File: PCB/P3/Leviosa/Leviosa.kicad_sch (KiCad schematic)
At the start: 56 parts, among them J1 Barrel_Jack, J2 2.54mm 1x03 Spare

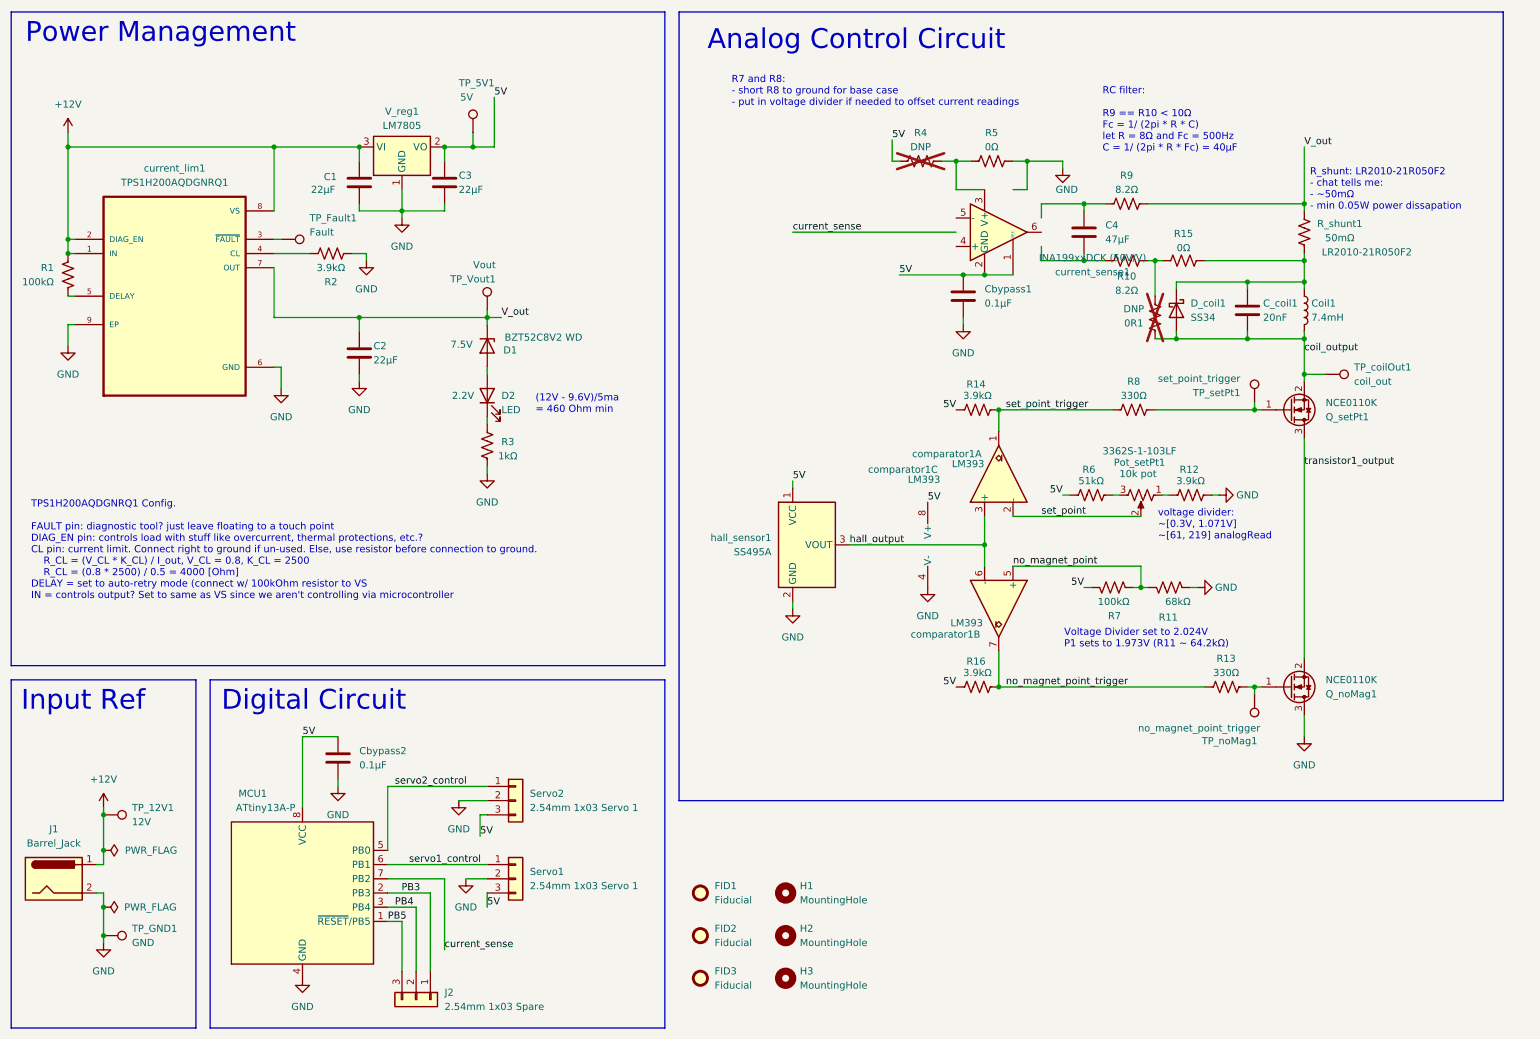
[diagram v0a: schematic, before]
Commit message: Pcb/p3 (#19)
* first pass on P3 of PCB

* shift parts in schematic

* update circuit with 0R on comparator output & servo pinout

* fix name

* add unity buffer op amp

* update schematic with single instrumental amplifier (instead of double)

* fix naming of folders

* update node names

* create PCB initial draft

* update PCB and schematic slightly

* Update - Dec 9th

- Updated labels for power, components and TPs
- Changed standard comp to 0603 knowing we have these
- Updated TPS symbol

* Board revised

- Big change from the last so have a look over

* added status led for coil and moved components groups closer together

* add 0.1uF cap to gate driver VCC

* update H1 pos

* add via

* gerbers created

* updated schematic for usb and i2s

* Update Leviosa.kicad_pro

---------

Co-authored-by: AirMatress <134566567+AirMatress@users.noreply.github.com>
Co-authored-by: Jack <134566567+Kay-Jack@users.noreply.github.com>
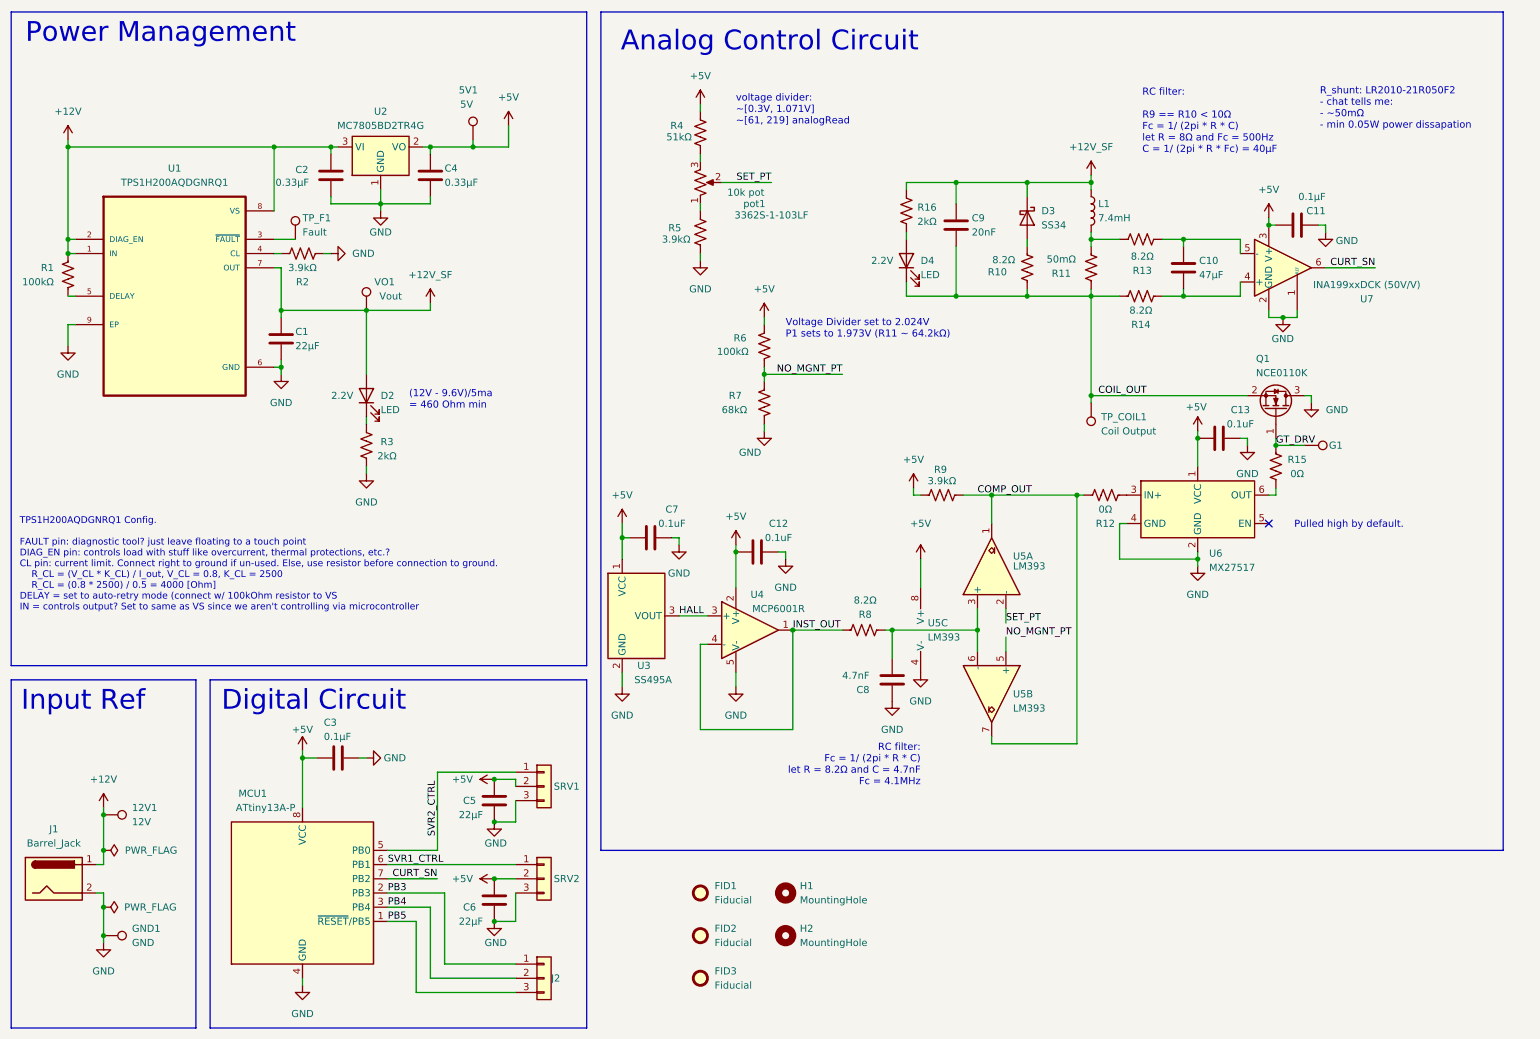
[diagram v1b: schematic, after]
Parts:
- removed 0R1, R4: DNP, Resistor_SMD:R_0603_1608Metric, symbol Device:R_US
- removed D1: BZT52C8V2 WD, Diode_SMD:D_SOD-123, symbol Device:D_Zener
- removed H3: MountingHole, MountingHole:MountingHole_3.2mm_M3_ISO7380, symbol Mechanical:MountingHole
- removed Q_noMag1: NCE0110K, Package_TO_SOT_SMD:TO-252-2, symbol Transistor_FET:DMN61D8LQ
- removed R13: 330Ω, Resistor_SMD:R_0805_2012Metric_Pad1.20x1.40mm_HandSolder, symbol Device:R_US
- removed R5: 0Ω, Resistor_SMD:R_0603_1608Metric, symbol Device:R_US
- removed TP_noMag1: no_magnet_point_trigger, TestPoint:TestPoint_Pad_D1.5mm, symbol Connector:TestPoint
- added C12, C13, C7: 0.1uF, Capacitor_SMD:C_0603_1608Metric, symbol Device:C
- added C5, C6: 22µF, Capacitor_SMD:C_0805_2012Metric, symbol Device:C
- added C8: 4.7nF, Capacitor_SMD:C_0805_2012Metric_Pad1.18x1.45mm_HandSolder, symbol Device:C
- added D4: LED, LED_SMD:LED_0805_2012Metric, symbol Device:LED
- added R10: 8.2Ω, Resistor_SMD:R_1206_3216Metric, symbol Device:R_US
- added R12: 0Ω, Resistor_SMD:R_0603_1608Metric, symbol Device:R_US
- added U4: MCP6001R, Package_TO_SOT_SMD:SOT-23-5, symbol Amplifier_Operational:MCP6001R
- added U6: MX27517, Package_TO_SOT_SMD:SOT-23-6, symbol Driver_FET:ZXGD3001E6
- 12V1: renamed from TP_12V1; footprint TestPoint:TestPoint_Pad_D1.5mm -> TestPoint:TestPoint_Pad_D1.0mm
- C11: renamed from Cbypass1; footprint Capacitor_SMD:C_0402_1005Metric -> Capacitor_SMD:C_0603_1608Metric
- C2: renamed from C1; value 22µF -> 0.33µF
- C3: renamed from Cbypass2; footprint Capacitor_SMD:C_0402_1005Metric -> Capacitor_SMD:C_0603_1608Metric
- C4: renamed from C3; value 22µF -> 0.33µF
- D3: renamed from D_coil1; footprint Diode_SMD:D_SMA -> Diode_SMD:D_SOD-323
- G1: renamed from TP_setPt1; footprint TestPoint:TestPoint_Pad_D1.5mm -> TestPoint:TestPoint_Pad_D1.0mm
- GND1: renamed from TP_GND1; footprint TestPoint:TestPoint_Pad_D1.5mm -> TestPoint:TestPoint_Pad_D1.0mm
- L1: renamed from Coil1; footprint Inductor_THT:L_Axial_L5.0mm_D3.6mm_P10.00mm_Horizontal_Murata_BL01RN1A2A2 -> Connector_PinHeader_2.54mm:PinHeader_2x01_P2.54mm_Vertical
- R1: footprint Resistor_SMD:R_0805_2012Metric_Pad1.20x1.40mm_HandSolder -> Resistor_SMD:R_0603_1608Metric
- R15: Link (none) -> https://jlcpcb.com/partdetail/18710-1206W4F820KT5E/C18022
- R16: value 3.9kΩ -> 2kΩ; Link https://jlcpcb.com/partdetail/23745-0603WAF3901T5E/C23018 -> (none)
- R3: value 1kΩ -> 2kΩ; footprint Resistor_SMD:R_0805_2012Metric_Pad1.20x1.40mm_HandSolder -> Resistor_SMD:R_0603_1608Metric
- R6: renamed from R7; footprint Resistor_SMD:R_0805_2012Metric_Pad1.20x1.40mm_HandSolder -> Resistor_SMD:R_0603_1608Metric
- R8: value 330Ω -> 8.2Ω; footprint Resistor_SMD:R_0805_2012Metric_Pad1.20x1.40mm_HandSolder -> Resistor_SMD:R_1206_3216Metric; Link (none) -> https://jlcpcb.com/partdetail/18710-1206W4F820KT5E/C18022
- TP_COIL1: renamed from TP_coilOut1; value coil_out -> Coil Output; footprint TestPoint:TestPoint_Pad_D1.5mm -> TestPoint:TestPoint_Pad_D1.0mm
- TP_F1: renamed from TP_Fault1; footprint TestPoint:TestPoint_Pad_D1.5mm -> TestPoint:TestPoint_Pad_D1.0mm
- U1: renamed from current_lim1; footprint TPS1H200AQDGNRQ1:SOP65P490X110-9N -> Package_SO:HVSSOP-8-1EP_3x3mm_P0.65mm_EP1.57x1.89mm; MF Texas Instruments -> (none); MP TPS1H200AQDGNRQ1 -> (none); PACKAGE HVSSOP-8 Texas Instruments -> (none); PRICE None -> (none); PURCHASE-URL https://www.snapeda.com/api/url_track_click_mouser/?unipart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 -> (none); SNAPEDA_LINK https://www.snapeda.com/parts/TPS1H200AQDGNRQ1/Texas+Instru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 -> (none)
- U2: renamed from V_reg1; value LM7805 -> MC7805BD2TR4G; footprint Package_TO_SOT_SMD:SOT-223-3_TabPin2 -> Package_TO_SOT_SMD:TO-263-2; Link (none) -> https://jlcpcb.com/partdetail/onsemi-MC7805BD2TR4G/C15833
- U5: renamed from comparator1; footprint Package_SO:SOIC-8_5.3x5.3mm_P1.27mm -> Package_SO:SOIC-8_3.9x4.9mm_P1.27mm; Link (none) -> https://jlcpcb.com/partdetail/onsemi-LM393DR2G/C7955
- VO1: renamed from TP_Vout1; footprint TestPoint:TestPoint_Pad_D1.5mm -> TestPoint:TestPoint_Pad_D1.0mm
- renumbered TP_5V1 to 5V1, C2 to C1, C4 to C10, C_coil1 to C9, Q_setPt1 to Q1, R_shunt1 to R11, R10 to R13, R9 to R14, R6 to R4, R12 to R5, R11 to R7, R14 to R9, Servo2 to SRV1, Servo1 to SRV2, hall_sensor1 to U3, current_sense1 to U7, Pot_setPt1 to pot1
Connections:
- net current_sense is gone; now on net CURT_SN: MCU1.7 (PB2)
- net transistor1_output is gone; now on net GND: Q1.3 (D)
- net GND: now also SRV1.3 (Pin_3), SRV2.3 (Pin_3), U7.1 (REF), U7.2 (GND), C12.2, C13.2, C5.2, C6.2, C7.2, C8.1, U4.5 (V-), U6.2 (GND), U6.4 (GND); no longer SRV1.2 (Pin_2), SRV2.2 (Pin_2)
- net at R13.1: now also L1.2, R11.1; no longer R15.2
- net at C10.2, R13.2: now also U7.5 (-)
- net +12V_SF: now reaches C9.1, D3.1 (K), L1.1
- net +12V_SF: now also C1.1, D2.2 (A), R16.1, U1.7 (OUT), VO1.1; no longer R11.1, R15.1
- net +5V: now reaches U7.3 (V+)
- net +5V: now also 5V1.1, C11.1, C3.1, C4.1, MCU1.8 (VCC), R4.2, R6.2, R9.2, SRV1.2 (Pin_2), SRV2.2 (Pin_2), U2.2 (VO), U3.1 (VCC), U5.8 (V+), C12.1, C13.1, C5.1, C6.1, C7.1, U4.2 (V+), U6.1 (VCC)
- net at U7.4 (+): now also C10.1, R14.2
- net CURT_SN: now reaches U7.6
- net GT_DRV: now reaches G1.1, Q1.1 (G)
- net GT_DRV: now also R15.2; no longer R8.1
- removed net 5V: 5V1.1, C11.1, C3.1, C4.1, MCU1.8 (VCC), R16.2, R4.2, R6.2, R9.2, SRV1.3 (Pin_3), SRV2.3 (Pin_3), U2.2 (VO), U3.1 (VCC), U5.8 (V+), U7.1 (REF), U7.2 (GND)
- removed net V_out: C1.1, R11.2, R14.1, U1.7 (OUT), VO1.1
- net coil_output renamed COIL_OUT
- net COIL_OUT: now also R11.2, R14.1, D4.1 (K), R10.2; no longer D3.2 (A), L1.2
- net hall_output: no longer names the net of U5.3 (+), U5.6 (-)
- net hall_output: now also R8.2, C8.2; no longer U3.3 (VOUT)
- net no_magnet_point renamed NO_MGNT_PT
- net no_magnet_point_trigger renamed COMP_OUT
- net COMP_OUT: now also R9.1, U5.1, R12.1; no longer R16.1
- net servo1_control renamed SVR1_CTRL
- net servo2_control renamed SVR2_CTRL
- net set_point renamed SET_PT
- removed net set_point_trigger: R8.2, R9.1, U5.1
- new net: D4.2 (A), R16.2
- new net: R12.2, U6.3 (IN+)
- new net: R15.1, U6.6 (OUT)
- new net: D3.2 (A), R10.1
- new net HALL: U3.3 (VOUT), U4.3 (+)
- new net INST_OUT: R8.1, U4.1, U4.4 (-)
- no-connect marks 0 -> 1
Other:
- note added: "Pulled high by default."
- note added: "RC filter: Fc = 1/ (2pi * R * C) let R = 8.2Ω and C = 4.7nF Fc = 4.1MHz"
- note removed: "R7 and R8: - short R8 to ground for base case - put in voltage divider if needed to offset current readings"
- moved on the sheet: 5V1, C1, C10, C11, C2, C3, C4, C9, D2, D3, G1, J2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
